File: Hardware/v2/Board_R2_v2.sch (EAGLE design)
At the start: 67 parts, among them U1 EDISON_CONNECTOR_FULLMOUNTING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, U2 LAN9512-JZX, U3 MAX4995AAUT+, U4 EDISON_CONNECTOR_FULLHEADER, U5 USD-SOCKETNEW, U6 TXB0108

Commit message: Changed PoE module to accomodate USB_VBUS, changed Rectifiers, added level shifter
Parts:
- removed AG9803MT: (no value), PoEdev:AG9800M
- added AG9805MT: (no value), PoEdev:AG9800M
- added C33, C34: 22uF, SparkFun-Capacitors:22UF-6.3V-20%(0805)
- added C35: 47pF, SparkFun-Capacitors:47PF-50V-5%(0603)
- added L3: 1.0uH, SparkFun-Passives:INDUCTOR1210
- added R18: 120K, SparkFun-Resistors:RESISTOR0402
- added U7: TPS62065, SparkFun-PowerIC:TPS62065
- B1, B2: value MB4S -> DF1510S; device rectifier:MB4S -> PoEdev:DF1510S
- R16: value 0 -> 680K; device resistor:R-US_R1210 -> SparkFun-Resistors:RESISTOR0402
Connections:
- new net N$32: C35.2, R16.1, R18.2, U7.FB
- net GND: now also AG9805MT.-VDC, C33.2, C34.2, R18.1, U7.AGND, U7.PAD, U7.PG, U7.PGND; no longer AG9803MT.-VDC, R16.2
- net N$14: now also L3.1, U7.SW; no longer AG9803MT.ADJ, R16.1
- net N$31: now also AG9805MT.VIN+1, AG9805MT.VIN+2; no longer AG9803MT.VIN+1, AG9803MT.VIN+2
- net N$33: now also AG9805MT.VIN-1, AG9805MT.VIN-2; no longer AG9803MT.VIN-1, AG9803MT.VIN-2
- net USB_VBUS: now also AG9805MT.+VDC1, AG9805MT.+VDC2, C30.1, C31.1, C32.1, C33.1, U7.AVIN, U7.EN, U7.PVIN
- net VSYS: now also C34.1, C35.1, L3.2, R16.2; no longer AG9803MT.+VDC1, AG9803MT.+VDC2, C30.1, C31.1, C32.1
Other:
- note added: "-----------------------REVISION NOTES"
- note added: "."
- note added: "3.2"
- note removed: "---------------------------------------REVISION NOTES"
- note removed: "3"
- note removed: "Fixed USB_ID and added test points"
- moved on the sheet: C1, C10, C11, C12, C15, C16, C17, C2, C28, C29, C3, C30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

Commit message: Tied DCIN to VSYS, added LED, cleaned up Bridge Rectifiers
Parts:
- added D2: BLUE, SparkFun-LED:LED-BLUE0603
- added R19: 1K, SparkFun-Resistors:1KOHM-1/10W-1%(0603)
- C33, C34: device SparkFun-Capacitors:22UF-6.3V-20%(0805) -> SparkFun-Capacitors:47PF-50V-5%(0603)
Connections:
- net N$27 renamed VB1
- net N$28 renamed VB2
- net N$29 renamed VA1
- net N$30 renamed VA2
- new net N$27: D2.C, R19.2
- net GND: now also R19.1
- net P14: no longer U1.DCIN
- net P4: no longer U1.VSYS@2
- net P6: no longer U1.VSYS@3
- net USB_VBUS: now also C34.1; no longer C33.1
- net VSYS: now also C33.1, D2.A, U1.DCIN, U1.VSYS@2, U1.VSYS@3; no longer C34.1
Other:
- note added: "3.3"
- note removed: "3.2"
- moved on the sheet: B1, B2, C33, C34, D1, RB1-125BHQ1A

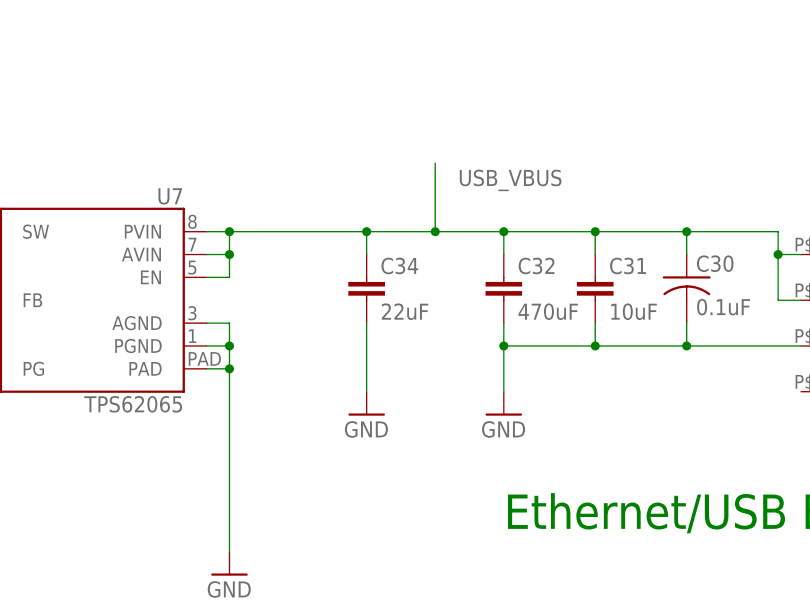
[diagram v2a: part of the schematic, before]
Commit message: Added R for min load
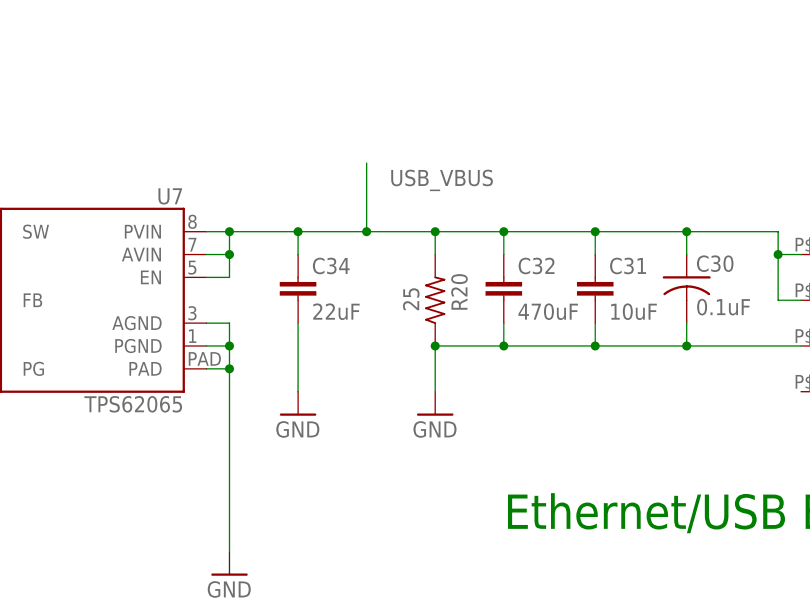
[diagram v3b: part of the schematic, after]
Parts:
- added R20: 25, resistor:R-US_R0402
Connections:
- net GND: now also R20.1
- net USB_VBUS: now also R20.2
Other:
- moved on the sheet: C34
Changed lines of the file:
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@@
 <part name="D2" library="SparkFun-LED" deviceset="LED-BLUE" device="0603" value="BLUE"/>
 <part name="GND30" library="supply1" deviceset="GND" device=""/>
+<part name="R20" library="resistor" deviceset="R-US_" device="R0402" value="25"/>
 </parts>
 <sheets>
@@
 <instance part="D1" gate="G$1" x="401.32" y="50.8" rot="R90"/>
 <instance part="C32" gate="G$1" x="327.66" y="55.88"/>
-<instance part="GND24" gate="1" x="327.66" y="40.64"/>
+<instance part="GND24" gate="1" x="320.04" y="40.64"/>
 <instance part="B1" gate="G$1" x="408.94" y="78.74" smashed="yes" rot="R180">
 <attribute name="VALUE" x="414.02" y="81.28" size="1.778" layer="96"/>
@@
 <attribute name="VALUE" x="256.54" y="63.5" size="1.778" layer="96"/>
 </instance>
-<instance part="GND25" gate="1" x="312.42" y="40.64"/>
+<instance part="GND25" gate="1" x="304.8" y="40.64"/>
 <instance part="GND26" gate="1" x="297.18" y="22.86"/>
 <instance part="GND27" gate="1" x="266.7" y="22.86"/>
@@
 <instance part="GND29" gate="1" x="218.44" y="22.86"/>
 <instance part="C33" gate="G$1" x="218.44" y="50.8"/>
-<instance part="C34" gate="G$1" x="312.42" y="53.34"/>
+<instance part="C34" gate="G$1" x="304.8" y="53.34"/>
 <instance part="R19" gate="G$1" x="203.2" y="40.64" rot="R90"/>
 <instance part="D2" gate="G$1" x="203.2" y="55.88"/>
 <instance part="GND30" gate="1" x="203.2" y="22.86"/>
+<instance part="R20" gate="G$1" x="320.04" y="53.34" smashed="yes" rot="R90">
+<attribute name="NAME" x="323.6214" y="52.07" size="1.778" layer="95" rot="R90"/>
+<attribute name="VALUE" x="318.262" y="52.07" size="1.778" layer="96" rot="R90"/>
+</instance>
 </instances>
 <busses>
@@
 </segment>
 <segment>
+<pinref part="U7" gate="G$1" pin="AGND"/>
+<pinref part="GND26" gate="1" pin="GND"/>
+<wire x1="294.64" y1="50.8" x2="297.18" y2="50.8" width="0.1524" layer="91"/>
+<wire x1="297.18" y1="50.8" x2="297.18" y2="48.26" width="0.1524" layer="91"/>
+<pinref part="U7" gate="G$1" pin="PGND"/>
+<wire x1="297.18" y1="48.26" x2="297.18" y2="45.72" width="0.1524" layer="91"/>
+<wire x1="297.18" y1="45.72" x2="297.18" y2="25.4" width="0.1524" layer="91"/>
+<wire x1="294.64" y1="48.26" x2="297.18" y2="48.26" width="0.1524" layer="91"/>
+<junction x="297.18" y="48.26"/>
+<pinref part="U7" gate="G$1" pin="PAD"/>
+<wire x1="294.64" y1="45.72" x2="297.18" y2="45.72" width="0.1524" layer="91"/>
+<junction x="297.18" y="45.72"/>
+</segment>
+<segment>
+<pinref part="U7" gate="G$1" pin="PG"/>
+<pinref part="GND27" gate="1" pin="GND"/>
+<wire x1="269.24" y1="45.72" x2="266.7" y2="45.72" width="0.1524" layer="91"/>
+<wire x1="266.7" y1="45.72" x2="266.7" y2="25.4" width="0.1524" layer="91"/>
+</segment>
+<segment>
+<pinref part="R18" gate="G$1" pin="1"/>
+<pinref part="GND28" gate="1" pin="GND"/>
+<wire x1="246.38" y1="30.48" x2="246.38" y2="25.4" width="0.1524" layer="91"/>
+</segment>
+<segment>
+<pinref part="GND25" gate="1" pin="GND"/>
+<wire x1="304.8" y1="50.8" x2="304.8" y2="43.18" width="0.1524" layer="91"/>
+<pinref part="C34" gate="G$1" pin="2"/>
+</segment>
+<segment>
+<pinref part="GND29" gate="1" pin="GND"/>
+<wire x1="218.44" y1="48.26" x2="218.44" y2="25.4" width="0.1524" layer="91"/>
+<pinref part="C33" gate="G$1" pin="2"/>
+</segment>
+<segment>
+<pinref part="R19" gate="G$1" pin="1"/>
+<pinref part="GND30" gate="1" pin="GND"/>
+<wire x1="203.2" y1="35.56" x2="203.2" y2="25.4" width="0.1524" layer="91"/>
+</segment>
+<segment>
 <pinref part="AG9805MT" gate="G$1" pin="-VDC"/>
 <wire x1="347.98" y1="48.26" x2="360.68" y2="48.26" width="0.1524" layer="91"/>
@@
 <wire x1="327.66" y1="48.26" x2="327.66" y2="50.8" width="0.1524" layer="91"/>
 <junction x="337.82" y="48.26"/>
-<wire x1="327.66" y1="48.26" x2="327.66" y2="43.18" width="0.1524" layer="91"/>
 <junction x="327.66" y="48.26"/>
+<pinref part="R20" gate="G$1" pin="1"/>
+<wire x1="320.04" y1="48.26" x2="327.66" y2="48.26" width="0.1524" layer="91"/>
 <pinref part="GND24" gate="1" pin="GND"/>
-</segment>
-<segment>
-<pinref part="U7" gate="G$1" pin="AGND"/>
-<pinref part="GND26" gate="1" pin="GND"/>
-<wire x1="294.64" y1="50.8" x2="297.18" y2="50.8" width="0.1524" layer="91"/>
-<wire x1="297.18" y1="50.8" x2="297.18" y2="48.26" width="0.1524" layer="91"/>
-<pinref part="U7" gate="G$1" pin="PGND"/>
-<wire x1="297.18" y1="48.26" x2="297.18" y2="45.72" width="0.1524" layer="91"/>
-<wire x1="297.18" y1="45.72" x2="297.18" y2="25.4" width="0.1524" layer="91"/>
-<wire x1="294.64" y1="48.26" x2="297.18" y2="48.26" width="0.1524" layer="91"/>
-<junction x="297.18" y="48.26"/>
-<pinref part="U7" gate="G$1" pin="PAD"/>
-<wire x1="294.64" y1="45.72" x2="297.18" y2="45.72" width="0.1524" layer="91"/>
-<junction x="297.18" y="45.72"/>
-</segment>
-<segment>
-<pinref part="U7" gate="G$1" pin="PG"/>
-<pinref part="GND27" gate="1" pin="GND"/>
-<wire x1="269.24" y1="45.72" x2="266.7" y2="45.72" width="0.1524" layer="91"/>
-<wire x1="266.7" y1="45.72" x2="266.7" y2="25.4" width="0.1524" layer="91"/>
-</segment>
-<segment>
-<pinref part="R18" gate="G$1" pin="1"/>
-<pinref part="GND28" gate="1" pin="GND"/>
-<wire x1="246.38" y1="30.48" x2="246.38" y2="25.4" width="0.1524" layer="91"/>
-</segment>
-<segment>
-<pinref part="GND25" gate="1" pin="GND"/>
-<wire x1="312.42" y1="50.8" x2="312.42" y2="43.18" width="0.1524" layer="91"/>
-<pinref part="C34" gate="G$1" pin="2"/>
-</segment>
-<segment>
-<pinref part="GND29" gate="1" pin="GND"/>
-<wire x1="218.44" y1="48.26" x2="218.44" y2="25.4" width="0.1524" layer="91"/>
-<pinref part="C33" gate="G$1" pin="2"/>
-</segment>
-<segment>
-<pinref part="R19" gate="G$1" pin="1"/>
-<pinref part="GND30" gate="1" pin="GND"/>
-<wire x1="203.2" y1="35.56" x2="203.2" y2="25.4" width="0.1524" layer="91"/>
+<wire x1="320.04" y1="43.18" x2="320.04" y2="48.26" width="0.1524" layer="91"/>
+<junction x="320.04" y="48.26"/>
 </segment>
 </net>
@@
 <wire x1="358.14" y1="53.34" x2="358.14" y2="58.42" width="0.1524" layer="91"/>
 <junction x="358.14" y="58.42"/>
-<wire x1="312.42" y1="58.42" x2="312.42" y2="60.96" width="0.1524" layer="91"/>
+<wire x1="304.8" y1="58.42" x2="304.8" y2="60.96" width="0.1524" layer="91"/>
+<wire x1="304.8" y1="60.96" x2="312.42" y2="60.96" width="0.1524" layer="91"/>
+<pinref part="U7" gate="G$1" pin="PVIN"/>
 <wire x1="312.42" y1="60.96" x2="320.04" y2="60.96" width="0.1524" layer="91"/>
-<pinref part="U7" gate="G$1" pin="PVIN"/>
 <wire x1="320.04" y1="60.96" x2="327.66" y2="60.96" width="0.1524" layer="91"/>
-<wire x1="312.42" y1="60.96" x2="297.18" y2="60.96" width="0.1524" layer="91"/>
-<junction x="312.42" y="60.96"/>
+<wire x1="304.8" y1="60.96" x2="297.18" y2="60.96" width="0.1524" layer="91"/>
+<junction x="304.8" y="60.96"/>
 <pinref part="U7" gate="G$1" pin="AVIN"/>
 <wire x1="297.18" y1="60.96" x2="294.64" y2="60.96" width="0.1524" layer="91"/>
@@
 <wire x1="297.18" y1="55.88" x2="297.18" y2="58.42" width="0.1524" layer="91"/>
 <junction x="297.18" y="58.42"/>
-<wire x1="320.04" y1="60.96" x2="320.04" y2="68.58" width="0.1524" layer="91"/>
+<wire x1="312.42" y1="60.96" x2="312.42" y2="68.58" width="0.1524" layer="91"/>
+<junction x="312.42" y="60.96"/>
+<label x="314.96" y="66.04" size="1.778" layer="95"/>
+<pinref part="C34" gate="G$1" pin="1"/>
+<pinref part="R20" gate="G$1" pin="2"/>
+<wire x1="320.04" y1="58.42" x2="320.04" y2="60.96" width="0.1524" layer="91"/>
 <junction x="320.04" y="60.96"/>
-<label x="322.58" y="66.04" size="1.778" layer="95"/>
-<pinref part="C34" gate="G$1" pin="1"/>
 </segment>
 </net>

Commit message: Added downstream USB through hirose, fixed some connections between top and bottom connectors
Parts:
- added C36: 22uF, SparkFun-Capacitors:47PF-50V-5%(0603)
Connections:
- removed net P12: U4.1.8V
- removed net P14: U4.DCIN
- removed net P2: U4.VSYS@1
- removed net P3: U4.USB_ID
- removed net P4: U4.VSYS@2
- removed net P6: U4.VSYS@3
- removed net USBUP: U4.USB_DP
- removed net USBUP2: U4.USB_DN
- new net USB_DN: U2.USBDM3, U4.USB_DN
- new net USB_DP: U2.USBDP3, U4.USB_DP
- net 1.8V: now also U4.1.8V
- net GND: now also C36.2, U4.USB_ID
- net USB_VBUS: now also C36.1
- net VSYS: now also U4.DCIN, U4.VSYS@1, U4.VSYS@2, U4.VSYS@3
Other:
- note added: "3.4"
- note added: "Added downstream USB through hirose"
- note removed: "."
- note removed: "3.3"
- moved on the sheet: C15, C16, C17, C18, R1, U4
